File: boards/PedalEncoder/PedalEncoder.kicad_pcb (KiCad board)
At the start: 2 copper layers, 125.1 x 38.1 mm, 33 parts, among them J1 Pwr, J2 Control, J3 Switch, J4 ISP, J5 Pedal, J6 MIDI Out, J7 I2C, Q1 BC547, U1 4069, U2 ATmega48-20P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

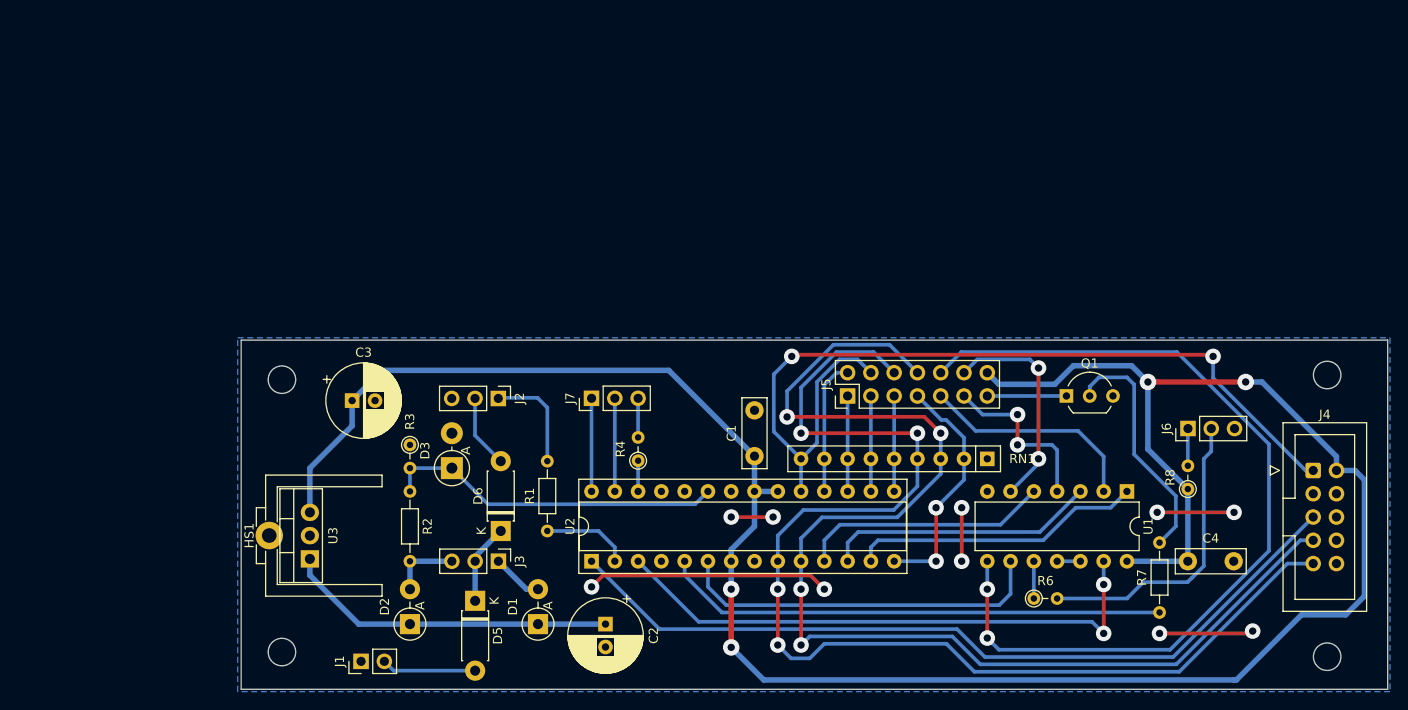
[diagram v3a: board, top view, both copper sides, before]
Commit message: Cleanup of PCB sizes and mounthole positions. Moved MIDI connectors to separate board.
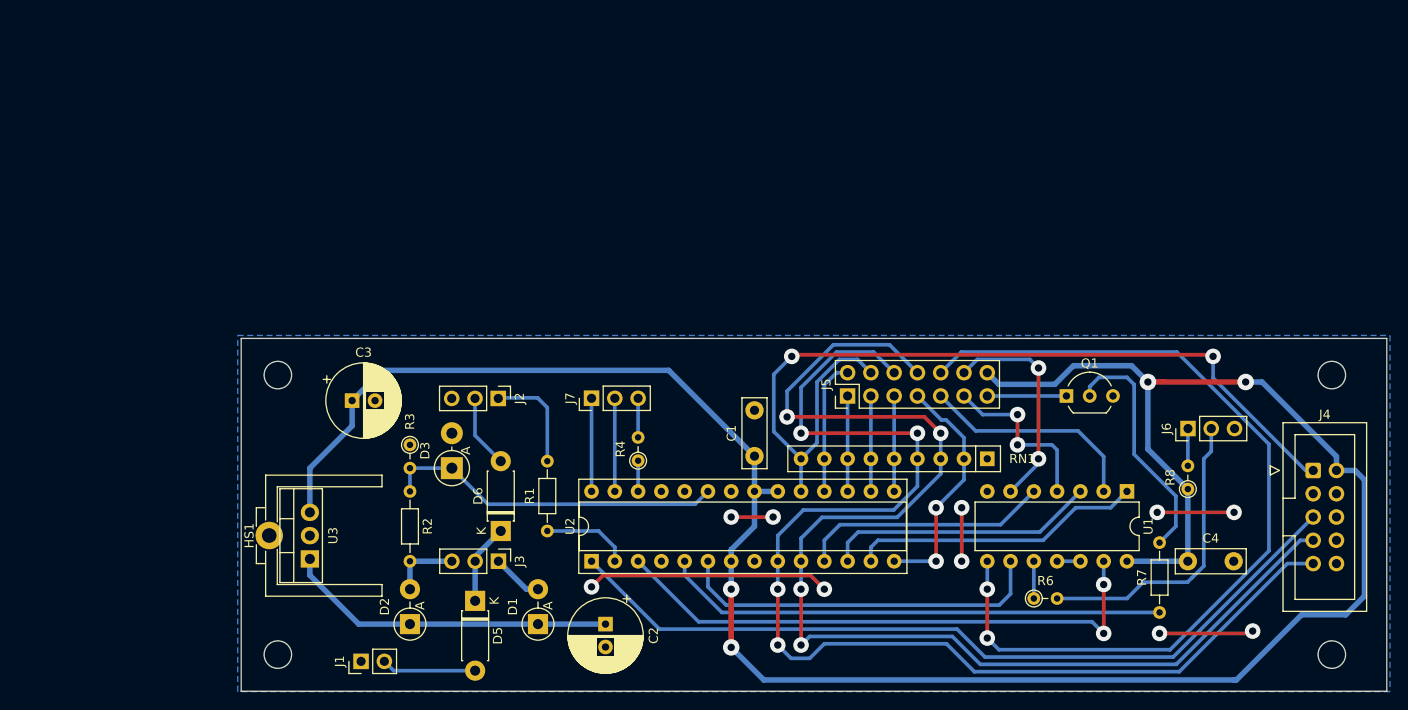
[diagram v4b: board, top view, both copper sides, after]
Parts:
- moved H1 0.67 mm to (74.0, 79.0)
- moved H4 0.56 mm to (189.0, 109.5)
- moved H2 0.53 mm to (74.0, 109.5)
- moved H3 0.51 mm to (189.0, 79.0)
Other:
- board size 125.1 x 38.1 mm -> 125 x 38.5 mm
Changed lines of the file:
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@@
 		(pad_to_mask_clearance 0)
 		(allow_soldermask_bridges_in_footprints no)
+		(aux_axis_origin 69.977 75)
 		(pcbplotparams
 			(layerselection 0x00010fc_ffffffff)
@@
 		(at 73.914 96.52 90)
 		(property "Reference" "HS1"
-			(at 0 -3.048 270)
+			(at 0 -3.048 -90)
 			(layer "F.SilkS")
 			(effects
@@
 		)
 		(property "Value" "Heatsink_Pad"
-			(at 0 12.446 270)
+			(at 0 12.446 -90)
 			(layer "F.Fab")
 			(effects
@@
 	(footprint "MountingHole:MountingHole_3mm"
 		(layer "F.Cu")
-		(at 74.422 79.502)
+		(at 73.977 79)
 		(descr "Mounting Hole 3mm, no annular")
 		(tags "mounting hole 3mm no annular")
@@
 	(footprint "MountingHole:MountingHole_3mm"
 		(layer "F.Cu")
-		(at 74.422 109.22)
+		(at 73.977 109.5)
 		(descr "Mounting Hole 3mm, no annular")
 		(tags "mounting hole 3mm no annular")
@@
 	(footprint "MountingHole:MountingHole_3mm"
 		(layer "F.Cu")
-		(at 188.468 109.728)
+		(at 188.977 109.5)
 		(descr "Mounting Hole 3mm, no annular")
 		(tags "mounting hole 3mm no annular")
@@
 	(footprint "MountingHole:MountingHole_3mm"
 		(layer "F.Cu")
-		(at 188.468 78.994)
+		(at 188.977 79)
 		(descr "Mounting Hole 3mm, no annular")
 		(tags "mounting hole 3mm no annular")
@@
 	)
 	(gr_rect
-		(start 69.977 75.184)
-		(end 195.072 113.284)
+		(start 69.977 75)
+		(end 194.977 113.5)
 		(stroke
 			(width 0.1)
@@
 		(layer "Edge.Cuts")
 	)
+	(dimension
+		(type orthogonal)
+		(layer "Cmts.User")
+		(pts
+			(xy 73.977 79) (xy 69.977 75)
+		)
+		(height -7.372)
+		(orientation 0)
+		(gr_text "4,0000 mm"
+			(at 71.977 70.478 0)
+			(layer "Cmts.User")
+			(effects
+				(font
+					(size 1 1)
+					(thickness 0.15)
+				)
+			)
+		)
+		(format
+			(prefix "")
+			(suffix "")
+			(units 3)
+			(units_format 1)
+			(precision 4)
+		)
+		(style
+			(thickness 0.1)
+			(arrow_length 1.27)
+			(text_position_mode 0)
+			(extension_height 0.58642)
+			(extension_offset 0.5) keep_text_aligned)
+	)
+	(dimension
+		(type orthogonal)
+		(layer "Cmts.User")
+		(pts
+			(xy 194.977 75) (xy 194.977 113.5)
+		)
+		(height 8.223)
+		(orientation 1)
+		(gr_text "38,5000 mm"
+			(at 202.05 94.25 90)
+			(layer "Cmts.User")
+			(effects
+				(font
+					(size 1 1)
+					(thickness 0.15)
+				)
+			)
+		)
+		(format
+			(prefix "")
+			(suffix "")
+			(units 3)
+			(units_format 1)
+			(precision 4)
+		)
+		(style
+			(thickness 0.1)
+			(arrow_length 1.27)
+			(text_position_mode 0)
+			(extension_height 0.58642)
+			(extension_offset 0.5) keep_text_aligned)
+	)
+	(dimension
+		(type orthogonal)
+		(layer "Cmts.User")
+		(pts
+			(xy 69.977 75) (xy 194.977 75)
+		)
+		(height -7.436)
+		(orientation 0)
+		(gr_text "125,0000 mm"
+			(at 132.477 66.414 0)
+			(layer "Cmts.User")
+			(effects
+				(font
+					(size 1 1)
+					(thickness 0.15)
+				)
+			)
+		)
+		(format
+			(prefix "")
+			(suffix "")
+			(units 3)
+			(units_format 1)
+			(precision 4)
+		)
+		(style
+			(thickness 0.1)
+			(arrow_length 1.27)
+			(text_position_mode 0)
+			(extension_height 0.58642)
+			(extension_offset 0.5) keep_text_aligned)
+	)
+	(dimension
+		(type orthogonal)
+		(layer "Cmts.User")
+		(pts
+			(xy 73.977 109.5) (xy 73.977 79)
+		)
+		(height -9.461)
+		(orientation 1)
+		(gr_text "30,5000 mm"
+			(at 63.366 94.25 90)
+			(layer "Cmts.User")
+			(effects
+				(font
+					(size 1 1)
+					(thickness 0.15)
+				)
+			)
+		)
+		(format
+			(prefix "")
+			(suffix "")
+			(units 3)
+			(units_format 1)
+			(precision 4)
+		)
+		(style
+			(thickness 0.1)
+			(arrow_length 1.27)
+			(text_position_mode 0)
+			(extension_height 0.58642)
+			(extension_offset 0.5) keep_text_aligned)
+	)
+	(dimension
+		(type orthogonal)
+		(layer "Cmts.User")
+		(pts
+			(xy 73.977 79) (xy 69.977 75)
+		)
+		(height -9.461)
+		(orientation 1)
+		(gr_text "4,0000 mm"
+			(at 63.366 77 90)
+			(layer "Cmts.User")
+			(effects
+				(font
+					(size 1 1)
+					(thickness 0.15)
+				)
+			)
+		)
+		(format
+			(prefix "")
+			(suffix "")
+			(units 3)
+			(units_format 1)
+			(precision 4)
+		)
+		(style
+			(thickness 0.1)
+			(arrow_length 1.27)
+			(text_position_mode 0)
+			(extension_height 0.58642)
+			(extension_offset 0.5) keep_text_aligned)
+	)
+	(dimension
+		(type orthogonal)
+		(layer "Cmts.User")
+		(pts
+			(xy 73.977 109.5) (xy 188.977 109.5)
+		)
+		(height 11.15)
+		(orientation 0)
+		(gr_text "115,0000 mm"
+			(at 131.477 119.5 0)
+			(layer "Cmts.User")
+			(effects
+				(font
+					(size 1 1)
+					(thickness 0.15)
+				)
+			)
+		)
+		(format
+			(prefix "")
+			(suffix "")
+			(units 3)
+			(units_format 1)
+			(precision 4)
+		)
+		(style
+			(thickness 0.1)
+			(arrow_length 1.27)
+			(text_position_mode 0)
+			(extension_height 0.58642)
+			(extension_offset 0.5) keep_text_aligned)
+	)
 	(segment
 		(start 110.744 97.79)
@@
 		(polygon
 			(pts
-				(xy 69.596 74.93) (xy 195.326 74.93) (xy 195.326 113.538) (xy 69.596 113.538)
+				(xy 69.596 74.676) (xy 195.326 74.676) (xy 195.326 113.538) (xy 69.596 113.538)
 			)
 		)

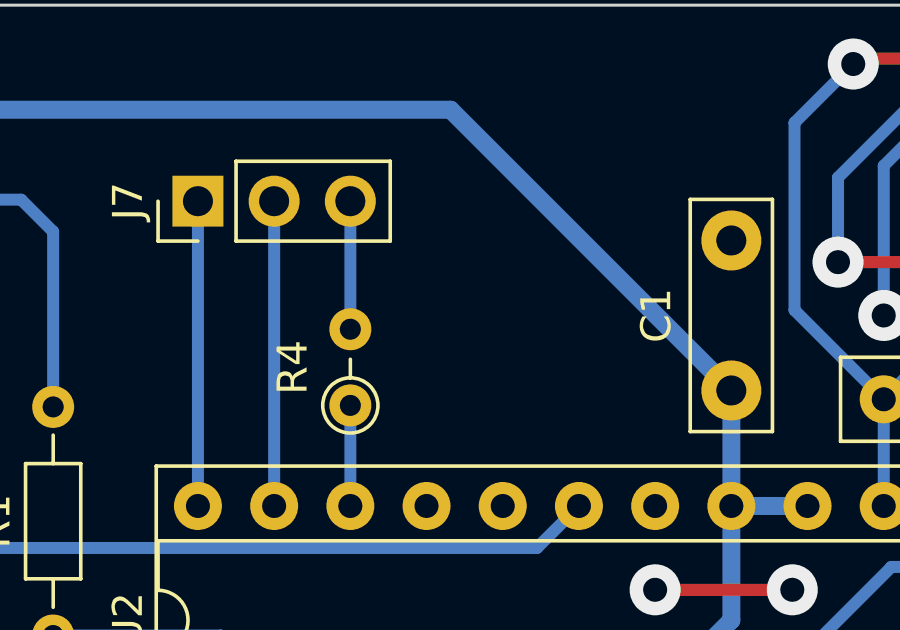
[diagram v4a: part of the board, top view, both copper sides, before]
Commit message: Fixed interrupt line to use open collector, added pullups to I2C lines
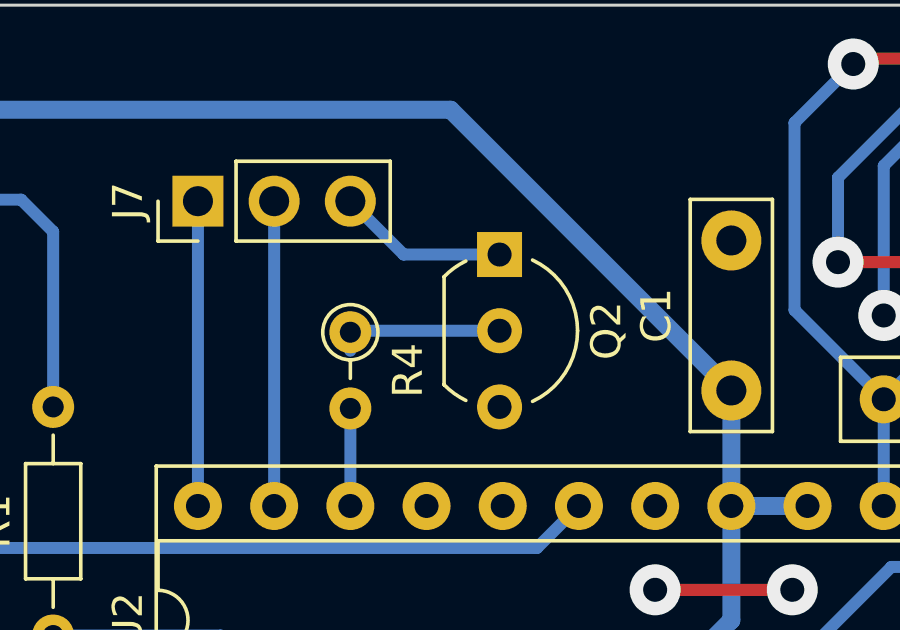
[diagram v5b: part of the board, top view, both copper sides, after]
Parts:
- added Q2: BC547, Package_TO_SOT_THT:TO-92_Inline_Wide, F.Cu at (118.3, 83.3)
- R4, R7: value 220 -> 4k7
- moved R4 2.44 mm to (113.3, 85.9), turned to -90 degrees
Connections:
- R4 pad 1: Interrupt -> Net-(Q2-B)
- R4 pad 2: Net-(J7-Pin_3) -> Interrupt
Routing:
- net Net-(Q2-B): track 0.00 -> 5.61 mm
- net Net-(J7-Pin_3): track 4.27 -> 5.71 mm

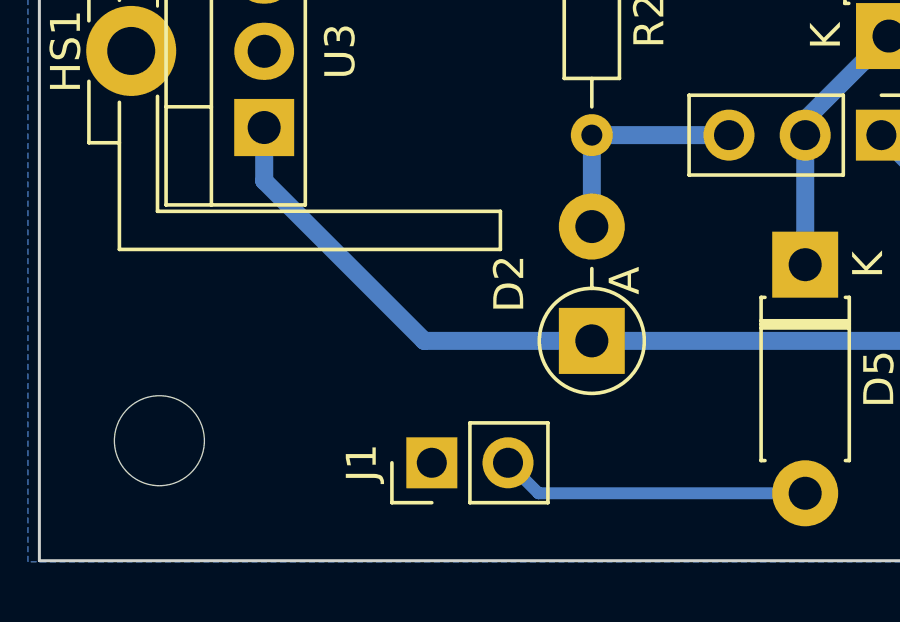
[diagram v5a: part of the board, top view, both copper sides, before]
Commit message: Added bypass caps to power supplies, use cheaper MAX232 IC.
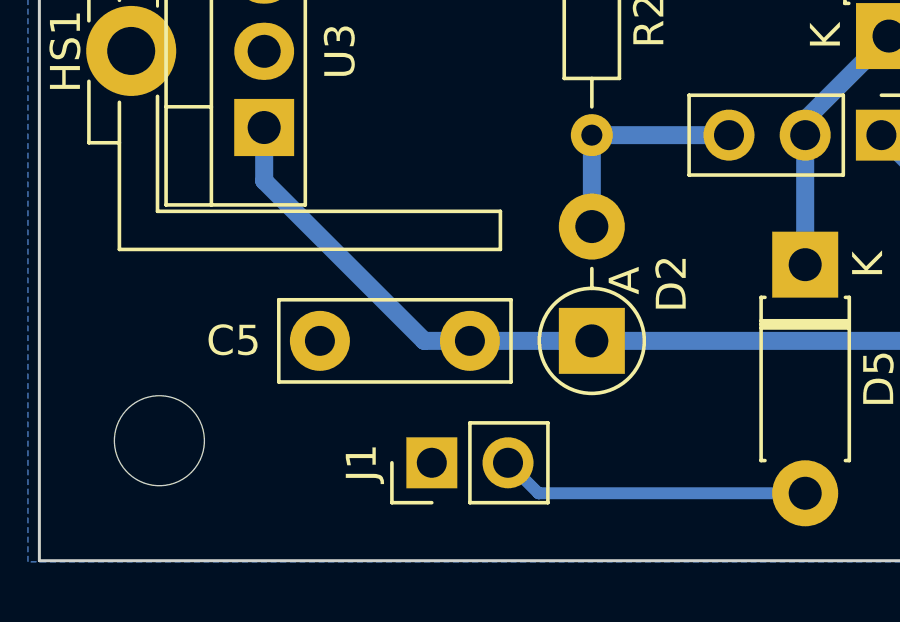
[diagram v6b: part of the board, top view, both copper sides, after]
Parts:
- added C5: 330nF, Capacitor_THT:C_Disc_D7.5mm_W2.5mm_P5.00mm, F.Cu at (84.3, 106.2)
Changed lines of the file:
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@@
+		)
+	)
+	(footprint "Capacitor_THT:C_Disc_D7.5mm_W2.5mm_P5.00mm"
+		(layer "F.Cu")
+		(at 84.328 106.172 180)
+		(descr "C, Disc series, Radial, pin pitch=5.00mm, , diameter*width=7.5*2.5mm^2, Capacitor, http://www.vishay.com/docs/28535/vy2series.pdf")
+		(tags "C Disc series Radial pin pitch 5.00mm  diameter 7.5mm width 2.5mm Capacitor")
+		(property "Reference" "C5"
+			(at 7.874 0 180)
+			(layer "F.SilkS")
+			(effects
+				(font
+					(size 1 1)
+					(thickness 0.15)
+				)
+			)
+		)
+		(property "Value" "330nF"
+			(at 2.5 2.5 180)
+			(layer "F.Fab")
+			(effects
+				(font
+					(size 1 1)
+					(thickness 0.15)
+				)
+			)
+		)
+		(property "Footprint" "Capacitor_THT:C_Disc_D7.5mm_W2.5mm_P5.00mm"
+			(at 0 0 180)
+			(unlocked yes)
+			(layer "F.Fab")
+			(hide yes)
+			(effects
+				(font
+					(size 1.27 1.27)
+				)
+			)
+		)
+		(property "Datasheet" ""
+			(at 0 0 180)
+			(unlocked yes)
+			(layer "F.Fab")
+			(hide yes)
+			(effects
+				(font
+					(size 1.27 1.27)
+				)
+			)
+		)
+		(property "Description" "Unpolarized capacitor"
+			(at 0 0 180)
+			(unlocked yes)
+			(layer "F.Fab")
+			(hide yes)
+			(effects
+				(font
+					(size 1.27 1.27)
+				)
+			)
+		)
+		(property ki_fp_filters "C_*")
+		(sheetname "Root")
+		(sheetfile "PedalEncoder.kicad_sch")
+		(attr through_hole)
+		(fp_line
+			(start 6.37 -1.37)
+			(end 6.37 1.37)
+			(stroke
+				(width 0.12)
+				(type solid)
+			)
+			(layer "F.SilkS")
+		)
+		(fp_line
+			(start -1.37 1.37)
+			(end 6.37 1.37)
+			(stroke
+				(width 0.12)
+				(type solid)
+			)
+			(layer "F.SilkS")
+		)
+		(fp_line
+			(start -1.37 -1.37)
+			(end 6.37 -1.37)
+			(stroke
+				(width 0.12)
+				(type solid)
+			)
+			(layer "F.SilkS")
+		)
+		(fp_line
+			(start -1.37 -1.37)
+			(end -1.37 1.37)
+			(stroke
+				(width 0.12)
+				(type solid)
+			)
+			(layer "F.SilkS")
+		)
+		(fp_line
+			(start 6.5 1.5)
+			(end 6.5 -1.5)
+			(stroke
+				(width 0.05)
+				(type solid)
+			)
+			(layer "F.CrtYd")
+		)
+		(fp_line
+			(start 6.5 -1.5)
+			(end -1.5 -1.5)
+			(stroke
+				(width 0.05)
+				(type solid)
+			)
+			(layer "F.CrtYd")
+		)
+		(fp_line
+			(start -1.5 1.5)
+			(end 6.5 1.5)
+			(stroke
+				(width 0.05)
+				(type solid)
+			)
+			(layer "F.CrtYd")
+		)
+		(fp_line
+			(start -1.5 -1.5)
+			(end -1.5 1.5)
+			(stroke
+				(width 0.05)
+				(type solid)
+			)
+			(layer "F.CrtYd")
+		)
+		(fp_line
+			(start 6.25 1.25)
+			(end 6.25 -1.25)
+			(stroke
+				(width 0.1)
+				(type solid)
+			)
+			(layer "F.Fab")
+		)
+		(fp_line
+			(start 6.25 -1.25)
+			(end -1.25 -1.25)
+			(stroke
+				(width 0.1)
+				(type solid)
+			)
+			(layer "F.Fab")
+		)
+		(fp_line
+			(start -1.25 1.25)
+			(end 6.25 1.25)
+			(stroke
+				(width 0.1)
+				(type solid)
+			)
+			(layer "F.Fab")
+		)
+		(fp_line
+			(start -1.25 -1.25)
+			(end -1.25 1.25)
+			(stroke
+				(width 0.1)
+				(type solid)
+			)
+			(layer "F.Fab")
+		)
+		(fp_text user "${REFERENCE}"
+			(at 2.5 0 180)
+			(layer "F.Fab")
+			(effects
+				(font
+					(size 1 1)
+					(thickness 0.15)
+				)
+			)
+		)
+		(pad "1" thru_hole circle
+			(at 0 0 180)
+			(size 2 2)
+			(drill 1)
+			(layers "*.Cu" "*.Mask")
+			(remove_unused_layers no)
+			(net 43 "/PWR_IN")
+			(pintype "passive")
+		)
+		(pad "2" thru_hole circle
+			(at 5 0 180)
+			(size 2 2)
+			(drill 1)
+			(layers "*.Cu" "*.Mask")
+			(remove_unused_layers no)
+			(net 5 "GND")
+			(pintype "passive")
+		)
+		(model "${KICAD8_3DMODEL_DIR}/Capacitor_THT.3dshapes/C_Disc_D7.5mm_W2.5mm_P5.00mm.wrl"
+			(offset
+				(xyz 0 0 0)
+			)
+			(scale
+				(xyz 1 1 1)
+			)
+			(rotate
+				(xyz 0 0 0)
+			)
 		)
 	)
@@
 		(tags "Diode DO-41_SOD81 series Axial Vertical pin pitch 3.81mm  length 5.2mm diameter 2.7mm")
 		(property "Reference" "D2"
-			(at 1.905 -2.750635 90)
+			(at 1.905 2.667 90)
 			(layer "F.SilkS")
 			(effects
@@
 		)
 		(fp_text user "${REFERENCE}"
-			(at 1.905 -2.750635 90)
-			(layer "F.Fab")
-			(effects
+			(at 1.905 2.667 90)
+			(layer "F.Fab")
+			(effects
